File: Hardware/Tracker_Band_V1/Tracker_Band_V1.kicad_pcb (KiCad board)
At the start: 4 copper layers, 19.2 x 25.9 mm, 57 parts, among them J1 USB_C_USB20, Q1 SSM6L56FE, SW1 EVP-AVAA1A, SW2 EVP-AVAA1A, U1 ESP32-C3-MINI-1-N4, U2 BNO085, U3 RT8010, U4 MCP73832-2-AC, U5 LM66200, U6 IN-PI15TAT5R5G5B, U7 IN-PI15TAT5R5G5B, U8 IN-PI15TAT5R5G5B, U9 IN-PI15TAT5R5G5B, X1 32.768kHz

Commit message: Initial layout finished
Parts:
- added LG1: ~, 00_tracker_fp:AB_logo, B.Cu at (145.5, 95.7)
- added TP1: 1.5mm, TestPoint:TestPoint_Pad_D1.5mm, B.Cu at (123.2, 100.4)
- added TP2: 1.5mm, TestPoint:TestPoint_Pad_D1.5mm, B.Cu at (125.7, 100.4)
- added TP3: 1.5mm, TestPoint:TestPoint_Pad_D1.5mm, B.Cu at (128.3, 100.4)
- added TP4: 1.5mm, TestPoint:TestPoint_Pad_D1.5mm, B.Cu at (130.8, 100.4)
- added TP5: 1.5mm, TestPoint:TestPoint_Pad_D1.5mm, B.Cu at (123.3, 79.4)
- added TP6: 1.5mm, TestPoint:TestPoint_Pad_D1.5mm, B.Cu at (123.3, 76.8)
- U4: value MCP73832-2-AC -> MCP73832
- X1: value 32.768kHz -> 32.768
- moved U8 16.5 mm to (139.9, 86.2)
- moved U9 16.5 mm to (123.5, 86.2)
- moved R23 1.00 mm to (123.7, 100.4), turned to 90 degrees
- moved R4 1.00 mm to (124.7, 100.4)
- moved R25 0.95 mm to (138.2, 88.2)
- moved R26 0.95 mm to (137.2, 88.2)
- moved R1 0.32 mm to (122.8, 89.8), turned to 90 degrees
- moved R16 0.18 mm to (124.0, 89.8)
- moved C8 0.17 mm to (125.9, 100.3)
- turned R19 to 180 degrees
- turned R20 to 180 degrees
- turned U6 to 180 degrees
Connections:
- R25 pad 2: Net-(U1-GPIO9) -> /BNO_CSn
- R26 pad 2: Net-(U1-GPIO8) -> /BNO_INTn
- R27 pad 2: Net-(U1-GPIO2,_ADC1_CH2,_FSPIQ) -> /RGB_LED
- SW1 pad 3: unconnected-(SW1-K-Pad3) -> Net-(SW1-A)
- U1 pad 12: unconnected-(U1-GPIO0,_ADC1_CH0,_XTAL_32K_P-Pad12) -> /SW_2
- U1 pad 13: unconnected-(U1-GPIO1,_ADC1_CH1,_XTAL_32K_N-Pad13) -> /CHRG_ST
- U1 pad 16: unconnected-(U1-GPIO10,_FSPICS0-Pad16) -> /OR_ST
- U1 pad 18: unconnected-(U1-GPIO4,_ADC1_CH4,_FSPIHD,_MTMS-Pad18) -> /BNO_MOSI
- U1 pad 19: unconnected-(U1-GPIO5,_ADC2_CH0,_FSPIWP,_MTDI-Pad19) -> /BNO_MISO
- U1 pad 20: unconnected-(U1-GPIO6,_FSPICLK,_MTCK-Pad20) -> /BNO_RSTn
- U1 pad 21: unconnected-(U1-GPIO7,_FSPID,_MTDO-Pad21) -> /BNO_SCLK
- U1 pad 22: Net-(U1-GPIO8) -> /BNO_INTn
- U1 pad 23: Net-(U1-GPIO9) -> /BNO_CSn
- U1 pad 30: unconnected-(U1-GPIO20,_U0RXD-Pad30) -> /BUCK_EN_MCU
- U1 pad 31: unconnected-(U1-GPIO21,_U0TXD-Pad31) -> /SW_1
- U1 pad 5: Net-(U1-GPIO2,_ADC1_CH2,_FSPIQ) -> /RGB_LED
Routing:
- net /OR_ST: track 0.38 -> 32.4 mm, vias 1 -> 3
- net /BUCK_EN: track 4.58 -> 36.1 mm, vias 0 -> 3
- net /RGB_LED3: track 0.00 -> 23.1 mm, vias 0 -> 2
- net /BNO_RSTn: track 0.00 -> 22.9 mm, vias 0 -> 2
- net /CHRG_ST: track 2.30 -> 24.8 mm, vias 0 -> 2
- net /BNO_CSn: track 0.00 -> 20.4 mm, vias 0 -> 2
- net VCC: track 0.00 -> 17.9 mm, vias 0 -> 2
- net /RGB_LED1: track 0.00 -> 16.8 mm, vias 0 -> 2
- net /BNO_MISO: track 0.00 -> 16.7 mm, vias 0 -> 2
- net /BNO_SCLK: track 0.00 -> 16.6 mm, vias 0 -> 2
- net /BNO_INTn: track 0.00 -> 16.5 mm, vias 0 -> 2
- net +3.3V: track 12.8 -> 28.3 mm, vias 9 -> 18
- net /USB_D-: track 0.58 -> 14.4 mm, vias 1 -> 2
- net /USB_D+: track 0.59 -> 14.0 mm, vias 1 -> 2
- net Net-(SW1-A): track 0.00 -> 12.4 mm, vias 0 -> 2
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- added copper zone on In2.Cu, net +3.3V
- added copper zone on In2.Cu, net +BATT
- added copper zone on B.Cu, net GND
- added copper zone on In1.Cu, net GND
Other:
- board text added: "3V3"
- board text added: "AN"
- board text added: "B+"
- board text added: "B-"
- board text added: "GND"
- board text added: "SCL"
- board text added: "SDA"

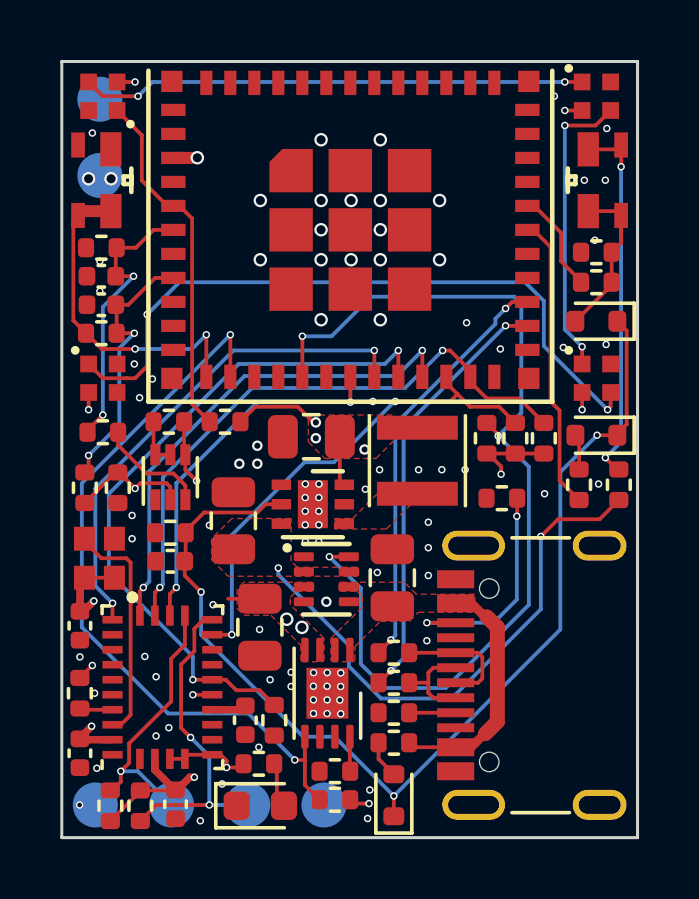
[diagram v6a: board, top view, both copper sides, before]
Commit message: DRC Corrected & TPs Added
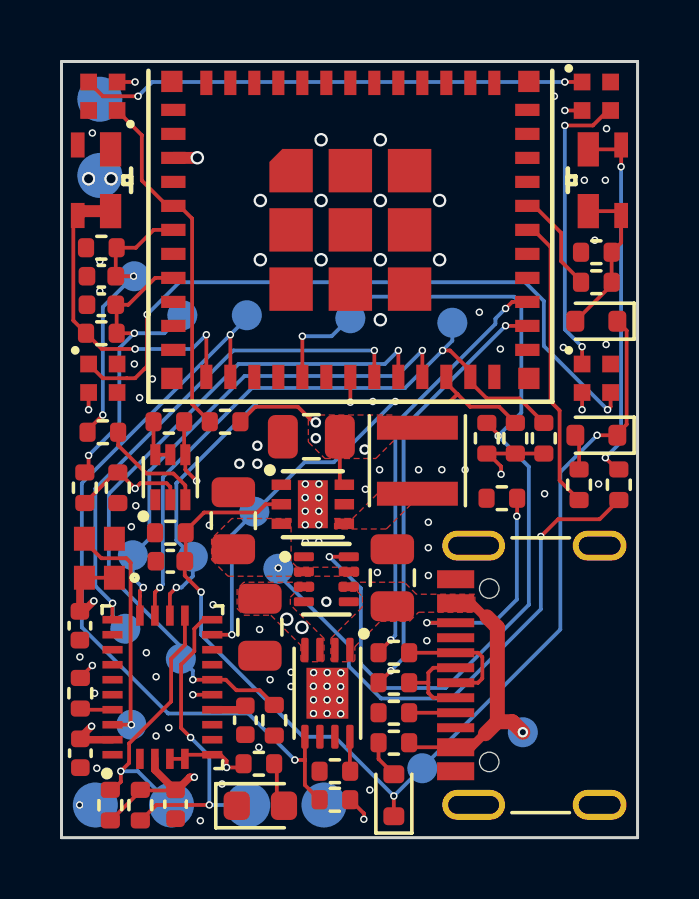
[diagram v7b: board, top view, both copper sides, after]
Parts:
- added TP10: 1mm, TestPoint:TestPoint_Pad_D1.0mm, B.Cu at (131.7, 84.2)
- added TP11: 1mm, TestPoint:TestPoint_Pad_D1.0mm, B.Cu at (134.1, 99.2)
- added TP12: 1mm, TestPoint:TestPoint_Pad_D1.0mm, B.Cu at (124.5, 82.8)
- added TP13: 1mm, TestPoint:TestPoint_Pad_D1.0mm, B.Cu at (126.1, 84.0)
- added TP14: 1mm, TestPoint:TestPoint_Pad_D1.0mm, B.Cu at (126.5, 92.1)
- added TP15: 1mm, TestPoint:TestPoint_Pad_D1.0mm, B.Cu at (124.2, 94.5)
- added TP16: 1mm, TestPoint:TestPoint_Pad_D1.0mm, B.Cu at (124.5, 92.0)
- added TP17: 1mm, TestPoint:TestPoint_Pad_D1.0mm, B.Cu at (135.1, 84.3)
- added TP18: 1mm, TestPoint:TestPoint_Pad_D1.0mm, B.Cu at (126.0, 95.5)
- added TP19: 1mm, TestPoint:TestPoint_Pad_D1.0mm, B.Cu at (128.5, 90.6)
- added TP20: 1mm, TestPoint:TestPoint_Pad_D1.0mm, B.Cu at (124.4, 97.7)
- added TP7: 1mm, TestPoint:TestPoint_Pad_D1.0mm, B.Cu at (137.4, 98.0)
- added TP8: 1mm, TestPoint:TestPoint_Pad_D1.0mm, B.Cu at (129.3, 92.5)
- added TP9: 1mm, TestPoint:TestPoint_Pad_D1.0mm, B.Cu at (128.2, 84.0)
- U4: value MCP73832 -> MCP73832-2-AC
- X1: value 32.768 -> 32.768kHz
- moved LG1 17.7 mm to (137.3, 80.0)
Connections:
- net Net-(U2-XIN32) renamed /XIN32
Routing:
- net /RST_N: track 9.17 -> 11.0 mm
- net +BATT: track 3.21 -> 2.15 mm
- net /BNO_CSn: track 20.4 -> 21.5 mm
- net /BNO_MISO: track 16.7 -> 17.7 mm
- net VBUS: track 8.43 -> 9.42 mm, vias 0 -> 1
- net /CHRG_ST: track 24.8 -> 25.7 mm
- net /BNO_MOSI: track 12.3 -> 12.8 mm
- net /XIN32: track 7.74 -> 7.96 mm, vias 0 -> 1
- net GND: vias 90 -> 84
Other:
- board text added: "2024"
- board text added: "JLCJLCJLCJLC"
- board text added: "SilhouetteSync V1"

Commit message: SCH & PCB Finalized for review
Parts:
- R19: value 10k -> 100k
- moved SW1 17.8 mm to (122.8, 79.5), turned to -90 degrees
- moved SW2 17.8 mm to (140.6, 79.5), turned to 90 degrees
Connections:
- SW2 pad 1: GND -> /SW_2
- SW2 pad 2: GND -> /SW_2
- SW2 pad 3: /SW_2 -> GND
- SW2 pad 4: /SW_2 -> GND
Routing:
- net /BUCK_EN_SW: track 5.31 -> 26.3 mm, vias 0 -> 2
- net /SW_2: track 11.1 -> 23.6 mm, vias 2 -> 4
- net Net-(SW1-A): track 12.4 -> 24.6 mm
- net /RGB_LED2: track 9.92 -> 8.90 mm
- net GND: vias 84 -> 81
- added copper zone on In2.Cu, net GND
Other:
- board text removed: "AN"
